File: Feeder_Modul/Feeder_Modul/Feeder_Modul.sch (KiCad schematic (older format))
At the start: 106 parts, among them J1 Conn_02x01, J101 Conn_02x01, J102 Conn_01x06_Male, J103 Conn_02x01, J104 Conn_02x01, J105 Conn_02x01, J106 WE_629104190121, J107 Conn_02x07_Odd_Even, J108 Conn_02x01, J109 Conn_02x01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

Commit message: Änderungen für bestellung V01 -  Bestellung abgeschickt
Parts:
- FID101, FID102, FID103: LCSC (none) -> 0
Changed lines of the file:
@@
 F 2 "Fiducial:Fiducial_1mm_Mask2mm" H 1000 8500 50  0001 C CNN
 F 3 "~" H 1000 8500 50  0001 C CNN
+F 4 "0" H 1000 8500 50  0001 C CNN "LCSC"
 	1    1000 8500
 	1    0    0    -1
@@
 F 2 "Fiducial:Fiducial_1mm_Mask2mm" H 1000 8750 50  0001 C CNN
 F 3 "~" H 1000 8750 50  0001 C CNN
+F 4 "0" H 1000 8750 50  0001 C CNN "LCSC"
 	1    1000 8750
 	1    0    0    -1
@@
 F 2 "Fiducial:Fiducial_1mm_Mask2mm" H 1000 9000 50  0001 C CNN
 F 3 "~" H 1000 9000 50  0001 C CNN
+F 4 "0" H 1000 9000 50  0001 C CNN "LCSC"
 	1    1000 9000
 	1    0    0    -1

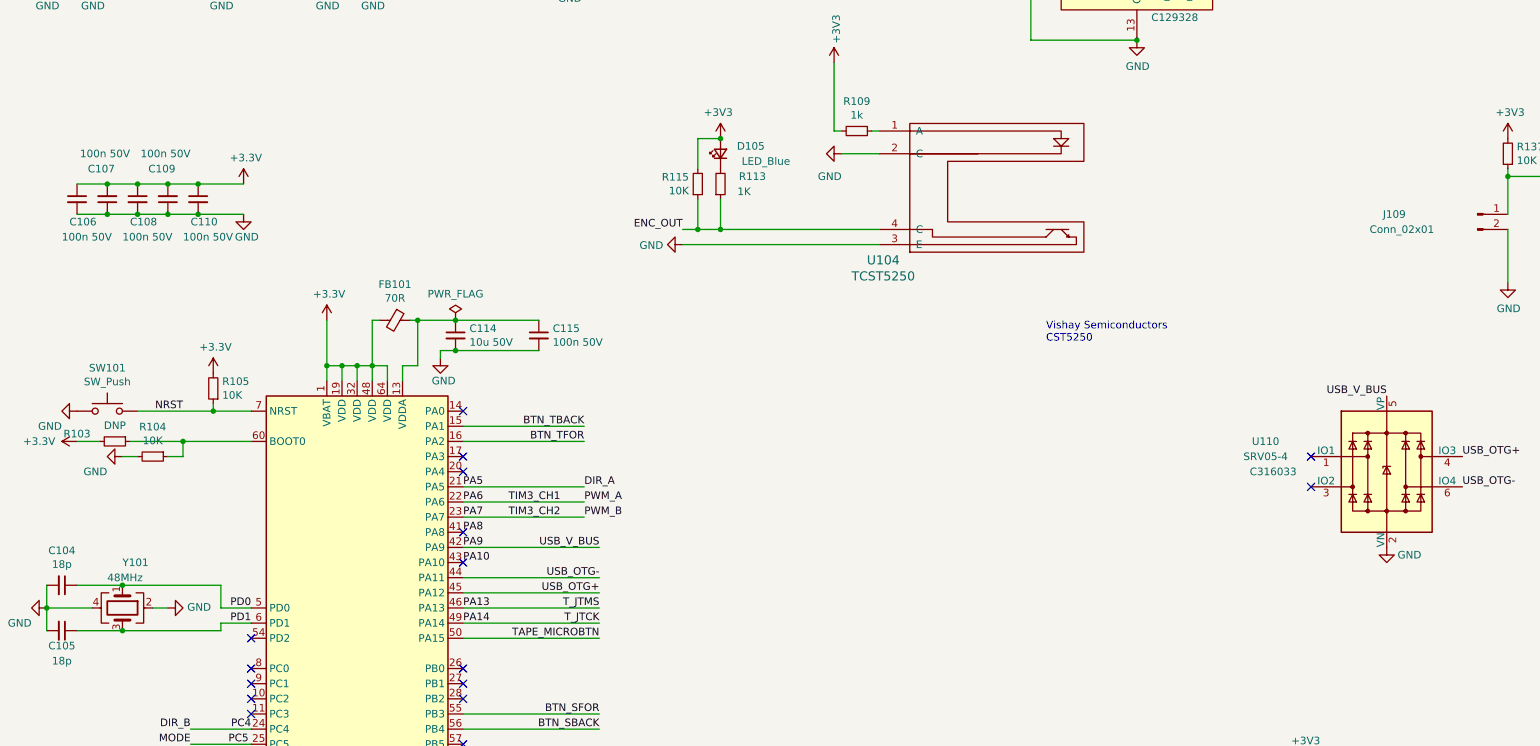
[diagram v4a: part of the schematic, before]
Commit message: Feeder Bugs behoben, Boards gebaut
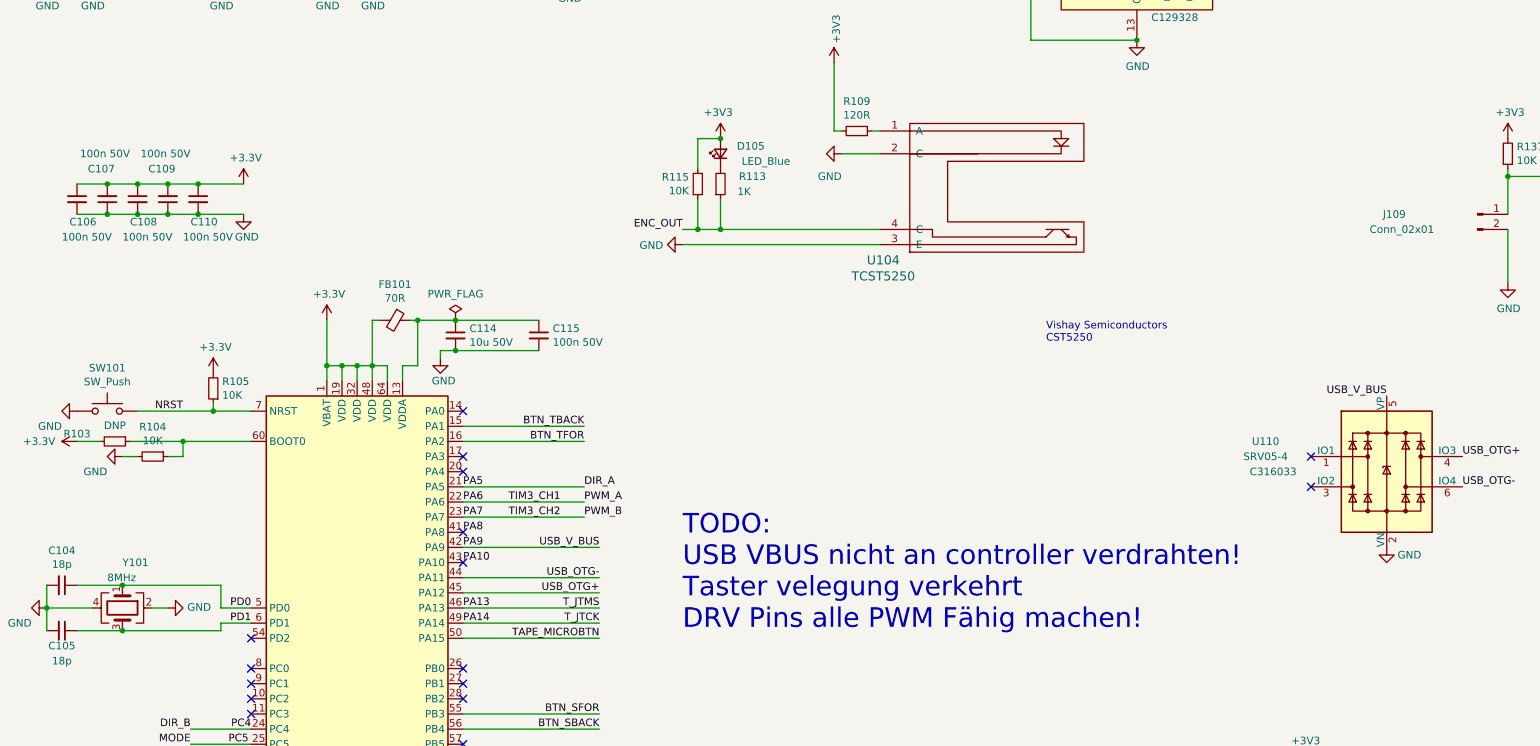
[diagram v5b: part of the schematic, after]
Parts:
- R109: value 1k -> 120R; LCSC C21190 -> C114681
- Y101: value 48MHz -> 8MHz; LCSC C389928 -> C400090
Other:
- note added: "TODO: \nUSB VBUS nicht an controller verdrahten!\nTaster velegung verkehrt\nDRV Pins alle PWM Fähig machen!"
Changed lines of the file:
@@
 P 7850 4000
 F 0 "R109" V 7654 4000 50  0000 C CNN
-F 1 "1k" V 7745 4000 50  0000 C CNN
+F 1 "120R" V 7745 4000 50  0000 C CNN
 F 2 "Resistor_SMD:R_0603_1608Metric" H 7850 4000 50  0001 C CNN
 F 3 "~" H 7850 4000 50  0001 C CNN
-F 4 "C21190" H 7850 4000 50  0001 C CNN "LCSC"
+F 4 "C114681" H 7850 4000 50  0001 C CNN "LCSC"
 	1    7850 4000
 	0    1    1    0
@@
 AR Path="/601BFBAA" Ref="Y101"  Part="1"
 F 0 "Y101" V 2700 7150 50  0000 L CNN
-F 1 "48MHz" V 2800 7050 50  0000 L CNN
+F 1 "8MHz" V 2800 7050 50  0000 L CNN
 F 2 "Crystal:Crystal_SMD_3225-4Pin_3.2x2.5mm" H 3000 7150 50  0001 C CNN
 F 3 "https://datasheet.lcsc.com/szlcsc/1907011833_XTY-7325-4800A1620-00_C389928.pdf" H 3000 7150 50  0001 C CNN
-F 4 "C389928" V 3000 7150 50  0001 C CNN "LCSC"
+F 4 "C400090" V 3000 7150 50  0001 C CNN "LCSC"
 	1    3000 7150
 	0    1    1    0
@@
 Wire Wire Line
 	13800 8800 13700 8800
+Text Notes 6700 7300 0    129  ~ 0
+TODO: \nUSB VBUS nicht an controller verdrahten!\nTaster velegung verkehrt\nDRV Pins alle PWM Fähig machen!
 $EndSCHEMATC

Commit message: Kleine Bugs im Feeder behoben, Löcher für Lagerhalter hinzugefügt
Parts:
- added R116, R138, R139, R140: 1k, Resistor_SMD:R_0603_1608Metric, symbol Device:R_Small
- SW101, SW102, SW103, SW104, SW105: symbol Switch:SW_Push -> PorjectLibrary:SW_Push
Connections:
- net +5V: no longer U102.42 (PA9)
- net BTN_SBACK: now also SW104.2; no longer SW104.1
- net BTN_SFOR: now also SW105.2; no longer SW105.1
- net BTN_TBACK: now also SW102.2; no longer SW102.1
- net BTN_TFOR: now also SW103.2; no longer SW103.1
- net DIR_B: no longer U105.8 (B_IN1_PH)
- net GND: now also SW101.3 (GND), SW102.1, SW102.3 (GND), SW103.1, SW103.3 (GND), SW104.1, SW104.3 (GND), SW105.1, SW105.3 (GND); no longer SW102.2, SW103.2, SW104.2, SW105.2
- net PA6: now also R116.2; no longer U105.9 (A_IN2_EN)
- net PA7: now also R138.1; no longer U105.7 (B_IN2_EN)
- net TIM3_CH3: now reaches U102.26 (PB0)
- net TIM3_CH3: now also R139.2
- net TIM3_CH4: now reaches U102.27 (PB1)
- net TIM3_CH4: now also R140.1
- net DIR_A: no longer names the net of U102.21 (PA5)
- net DIR_A: no longer U105.10 (A_IN1_PH)
- new net PWM_A: R116.1, U105.10 (A_IN1_PH)
- new net PWM_B: R138.2, U105.9 (A_IN2_EN)
- new net PWM_C: R139.1, U105.8 (B_IN1_PH)
- new net PWM_D: R140.2, U105.7 (B_IN2_EN)
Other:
- moved on the sheet: U110
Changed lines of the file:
@@
 MODE
 Text Label 10850 2700 0    50   ~ 0
-DIR_A
-Text Label 10850 2800 0    50   ~ 0
 PWM_A
-Text Label 10850 3000 0    50   ~ 0
-DIR_B
-Text Label 10850 3100 0    50   ~ 0
+Text Label 10850 2800 0    50   ~ 0
 PWM_B
 Wire Wire Line
@@
 $EndComp
 $Comp
-L Switch:SW_Push SW102
+L PorjectLibrary:SW_Push SW102
 U 1 1 6010EF5E
 P 14050 1950
@@
 F 4 "C455137" H 14050 1950 50  0001 C CNN "LCSC"
 	1    14050 1950
-	1    0    0    -1
+	-1   0    0    -1
 $EndComp
 $Comp
@@
 $EndComp
 $Comp
-L Switch:SW_Push SW103
+L PorjectLibrary:SW_Push SW103
 U 1 1 6010F6AA
 P 14050 2450
@@
 F 4 "C455137" H 0   0   50  0001 C CNN "LCSC"
 	1    14050 2450
-	1    0    0    -1
+	-1   0    0    -1
 $EndComp
 $Comp
@@
 $EndComp
 $Comp
-L Switch:SW_Push SW104
+L PorjectLibrary:SW_Push SW104
 U 1 1 6010F718
 P 14050 2900
@@
 F 4 "C455137" H 0   0   50  0001 C CNN "LCSC"
 	1    14050 2900
-	1    0    0    -1
+	-1   0    0    -1
 $EndComp
 Wire Wire Line
@@
 $EndComp
 $Comp
-L Switch:SW_Push SW105
+L PorjectLibrary:SW_Push SW105
 U 1 1 60119529
 P 14050 3400
@@
 F 4 "C455137" H 0   0   50  0001 C CNN "LCSC"
 	1    14050 3400
-	1    0    0    -1
+	-1   0    0    -1
 $EndComp
 Wire Wire Line
@@
 Wire Wire Line
 	14200 6200 14050 6200
-Text Label 12900 5900 2    50   ~ 0
-USB_V_BUS
 Wire Wire Line
 	14200 5900 13450 5900
-Text Label 6150 6750 2    50   ~ 0
-USB_V_BUS
 Text Label 6150 7050 2    50   ~ 0
 USB_OTG+
@@
 Wire Wire Line
 	5250 7050 6150 7050
-Wire Wire Line
-	6150 6750 5250 6750
-Text Label 5250 6750 0    50   ~ 0
-PA9
 Text Label 5250 6850 0    50   ~ 0
 PA10
@@
 CAN1_L
 $Comp
-L Switch:SW_Push SW101
+L PorjectLibrary:SW_Push SW101
 U 1 1 60519E5E
 P 2900 5850
@@
 Wire Wire Line
 	13450 6650 13450 6300
-Wire Wire Line
-	12900 5900 13450 5900
 Text Label 5250 6650 0    50   ~ 0
 PA8
@@
 Wire Wire Line
 	5250 8750 5650 8750
-Text Label 5250 6350 0    50   ~ 0
-PA5
-Text Label 6050 6350 0    50   ~ 0
-DIR_A
 Text Label 5250 6450 0    50   ~ 0
 PA6
 Text Label 5550 6450 0    50   ~ 0
 TIM3_CH1
-Text Label 6050 6450 0    50   ~ 0
+Text Label 6650 6450 0    50   ~ 0
 PWM_A
 Text Label 5250 6550 0    50   ~ 0
@@
 Text Label 5550 6550 0    50   ~ 0
 TIM3_CH2
-Text Label 6050 6550 0    50   ~ 0
+Text Label 6650 6550 0    50   ~ 0
 PWM_B
 Text Label 3850 7950 2    50   ~ 0
@@
 Wire Wire Line
 	3850 7950 3450 7950
-Wire Wire Line
-	6050 6350 5250 6350
-Wire Wire Line
-	5250 6450 6050 6450
-Wire Wire Line
-	6050 6550 5250 6550
 $Comp
 L Device:R_Small R129
@@
 	9200 10000 9200 10050
 Connection ~ 9200 10050
-NoConn ~ 5250 7550
-NoConn ~ 5250 7650
 NoConn ~ 5250 7750
 NoConn ~ 5250 8050
@@
 L Power_Protection:SRV05-4 U110
 U 1 1 60371E49
-P 11350 6250
-F 0 "U110" H 10550 6450 50  0000 C CNN
-F 1 "SRV05-4" H 10550 6350 50  0000 C CNN
-F 2 "Package_TO_SOT_SMD:SOT-23-6" H 12050 5800 50  0001 C CNN
-F 3 "http://www.onsemi.com/pub/Collateral/SRV05-4-D.PDF" H 11350 6250 50  0001 C CNN
-F 4 "C316033" H 10600 6250 50  0000 C CNN "LCSC"
-	1    11350 6250
+P 12350 6600
+F 0 "U110" H 11550 6800 50  0000 C CNN
+F 1 "SRV05-4" H 11550 6700 50  0000 C CNN
+F 2 "Package_TO_SOT_SMD:SOT-23-6" H 13050 6150 50  0001 C CNN
+F 3 "http://www.onsemi.com/pub/Collateral/SRV05-4-D.PDF" H 12350 6600 50  0001 C CNN
+F 4 "C316033" H 11600 6600 50  0000 C CNN "LCSC"
+	1    12350 6600
 	1    0    0    -1
 $EndComp
@@
 L power:GND #PWR?
 U 1 1 60371E4F
-P 11350 6750
+P 12350 7100
 AR Path="/5FDD0F66/60371E4F" Ref="#PWR?"  Part="1"
 AR Path="/60371E4F" Ref="#PWR0135"  Part="1"
-F 0 "#PWR0135" H 11350 6500 50  0001 C CNN
-F 1 "GND" H 11500 6700 50  0000 C CNN
-F 2 "" H 11350 6750 50  0001 C CNN
-F 3 "" H 11350 6750 50  0001 C CNN
-	1    11350 6750
+F 0 "#PWR0135" H 12350 6850 50  0001 C CNN
+F 1 "GND" H 12500 7050 50  0000 C CNN
+F 2 "" H 12350 7100 50  0001 C CNN
+F 3 "" H 12350 7100 50  0001 C CNN
+	1    12350 7100
 	1    0    0    -1
 $EndComp
-Text Label 11350 5750 2    50   ~ 0
-USB_V_BUS
-Text Label 11850 6150 0    50   ~ 0
+Text Label 12850 6500 0    50   ~ 0
 USB_OTG+
-Text Label 11850 6350 0    50   ~ 0
+Text Label 12850 6700 0    50   ~ 0
 USB_OTG-
-NoConn ~ 10850 6150
-NoConn ~ 10850 6350
+NoConn ~ 11850 6500
+NoConn ~ 11850 6700
 $Comp
 L Mechanical:Fiducial FID101
@@
 Wire Wire Line
 	13800 8800 13700 8800
-Text Notes 6700 7300 0    129  ~ 0
+Text Notes 7600 8650 0    129  ~ 0
 TODO: \nUSB VBUS nicht an controller verdrahten!\nTaster velegung verkehrt\nDRV Pins alle PWM Fähig machen!
+NoConn ~ 5250 6750
+Wire Wire Line
+	2700 5950 2700 5850
+Connection ~ 2700 5850
+Wire Wire Line
+	14250 2050 14250 1950
+Connection ~ 14250 1950
+Wire Wire Line
+	14250 2550 14250 2450
+Connection ~ 14250 2450
+Wire Wire Line
+	14250 3000 14250 2900
+Connection ~ 14250 2900
+Wire Wire Line
+	14250 3500 14250 3400
+Connection ~ 14250 3400
+Text Label 5550 7550 0    50   ~ 0
+TIM3_CH3
+Text Label 5550 7650 0    50   ~ 0
+TIM3_CH4
+Text Label 6650 7550 0    50   ~ 0
+PWM_C
+Text Label 6650 7650 0    50   ~ 0
+PWM_D
+Text Label 10850 3000 0    50   ~ 0
+PWM_C
+Text Label 10850 3100 0    50   ~ 0
+PWM_D
+$Comp
+L Device:R_Small R138
+U 1 1 60937A80
+P 6350 6550
+F 0 "R138" V 6154 6550 50  0000 C CNN
+F 1 "1k" V 6245 6550 50  0000 C CNN
+F 2 "Resistor_SMD:R_0603_1608Metric" H 6350 6550 50  0001 C CNN
+F 3 "~" H 6350 6550 50  0001 C CNN
+F 4 "C21190" H 6350 6550 50  0001 C CNN "LCSC"
+	1    6350 6550
+	0    -1   -1   0
+$EndComp
+NoConn ~ 5250 6350
+$Comp
+L Device:R_Small R116
+U 1 1 6095D218
+P 6350 6450
+F 0 "R116" V 6154 6450 50  0000 C CNN
+F 1 "1k" V 6245 6450 50  0000 C CNN
+F 2 "Resistor_SMD:R_0603_1608Metric" H 6350 6450 50  0001 C CNN
+F 3 "~" H 6350 6450 50  0001 C CNN
+F 4 "C21190" H 6350 6450 50  0001 C CNN "LCSC"
+	1    6350 6450
+	0    1    1    0
+$EndComp
+Wire Wire Line
+	6650 6450 6450 6450
+Wire Wire Line
+	6450 6550 6650 6550
+Wire Wire Line
+	5250 6450 6250 6450
+Wire Wire Line
+	5250 6550 6250 6550
+$Comp
+L Device:R_Small R140
+U 1 1 60A0F3C9
+P 6350 7650
+F 0 "R140" V 6154 7650 50  0000 C CNN
+F 1 "1k" V 6245 7650 50  0000 C CNN
+F 2 "Resistor_SMD:R_0603_1608Metric" H 6350 7650 50  0001 C CNN
+F 3 "~" H 6350 7650 50  0001 C CNN
+F 4 "C21190" H 6350 7650 50  0001 C CNN "LCSC"
+	1    6350 7650
+	0    -1   -1   0
+$EndComp
+$Comp
+L Device:R_Small R139
+U 1 1 60A0F9AC
+P 6350 7550
+F 0 "R139" V 6154 7550 50  0000 C CNN
+F 1 "1k" V 6245 7550 50  0000 C CNN
+F 2 "Resistor_SMD:R_0603_1608Metric" H 6350 7550 50  0001 C CNN
+F 3 "~" H 6350 7550 50  0001 C CNN
+F 4 "C21190" H 6350 7550 50  0001 C CNN "LCSC"
+	1    6350 7550
+	0    1    1    0
+$EndComp
+Wire Wire Line
+	6650 7550 6450 7550
+Wire Wire Line
+	5250 7550 6250 7550
+Wire Wire Line
+	5250 7650 6250 7650
+Wire Wire Line
+	6450 7650 6650 7650
+Wire Wire Line
+	12350 5900 12350 6100
+Wire Wire Line
+	12350 5900 13450 5900
 $EndSCHEMATC
